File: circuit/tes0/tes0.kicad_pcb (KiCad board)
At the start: 2 copper layers, 21 parts, among them U1 SIM7000E

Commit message: sim7000e minus antena
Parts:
- added J-S70_USIM1: SIM_Card, Connector_Card:microSIM_JAE_SF53S006VCBR2000, F.Cu at (208.7, 116.6)
- moved J-USB-S70 3.43 mm to (189.7, 120.2)
- moved R-S70_USB2 3.35 mm to (190.1, 112.5)
- moved R-S70_USB3 3.35 mm to (188.0, 112.5)
- moved SW-S70-PWR1 3.35 mm to (179.0, 114.9)
- moved SW-S70-RST1 3.35 mm to (168.4, 115.0)
- moved R-S70_USB1 3.35 mm to (192.1, 112.5)
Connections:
- JIO-S3 pad 1: Net-(JIO-S3-Pad1) -> /USIM_VPP
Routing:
- net /S70_USIM_CLK: track 19.3 -> 55.8 mm, vias 0 -> 2
- net /USIM_VPP: track 0.00 -> 34.6 mm
- net /S70_USIM_DATA: track 18.3 -> 46.4 mm, vias 0 -> 2
- net /S70_USIM_VDD: track 17.1 -> 33.6 mm
- net /S70_USIM_RST: track 20.8 -> 36.9 mm
- net GND: track 333.1 -> 347.4 mm
- net /S70_VDD: track 131.4 -> 136.3 mm
- net /S70_USB_DM: track 22.2 -> 25.9 mm
- net /S70_USB_DP: track 24.1 -> 21.1 mm
- net /S70_USB_VBUS: track 32.3 -> 30.7 mm
- net /S70_NRST: track 40.4 -> 38.9 mm
- net Net-(J-USB-S70-Pad2): track 4.04 -> 5.27 mm
- net Net-(J-USB-S70-Pad3): track 5.92 -> 7.10 mm
- net /S70_PWRKEY: track 95.2 -> 94.1 mm
- added copper zone on B.Cu, net (none)
- added copper zone on F.Cu, net (none)
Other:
- board outline added: 66 x 76.4 mm

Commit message: add FT232RL
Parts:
- added C-AMS1: 100nF, Capacitor_SMD:C_0805_2012Metric_Pad1.15x1.40mm_HandSolder, B.Cu at (139.2, 108.1)
- added C-AMS2: 100nF, Capacitor_SMD:C_0805_2012Metric_Pad1.15x1.40mm_HandSolder, B.Cu at (132.8, 108.3)
- added C-FT_3V3: 100nF, Capacitor_SMD:C_0805_2012Metric_Pad1.15x1.40mm_HandSolder, B.Cu at (151.1, 109.4)
- added D-FT_RXD1: LED, LED_SMD:LED_1206_3216Metric_Pad1.42x1.75mm_HandSolder, F.Cu at (141.6, 99.1)
- added D-FT_TXD1: LED, LED_SMD:LED_1206_3216Metric_Pad1.42x1.75mm_HandSolder, F.Cu at (144.2, 99.1)
- added J-BRD_S70_FT1: Conn_02x02_Odd_Even, Connector_PinHeader_2.54mm:PinHeader_2x02_P2.54mm_Vertical, F.Cu at (148.8, 81.4)
- added J-BRD_VDD1: Conn_02x04_Odd_Even, Connector_PinHeader_2.54mm:PinHeader_2x04_P2.54mm_Vertical, F.Cu at (151.1, 52.2)
- added J-FT_USB1: USB_B_Micro, Connector_USB:USB_Micro-B_Wuerth_629105150521, F.Cu at (148.5, 119.7)
- added R-FT_RXD1: 330, Resistor_SMD:R_0805_2012Metric_Pad1.15x1.40mm_HandSolder, B.Cu at (144.2, 99.6)
- added R-FT_TXD1: 330, Resistor_SMD:R_0805_2012Metric_Pad1.15x1.40mm_HandSolder, B.Cu at (141.7, 99.5)
- added U2: FT232RL, Package_SO:SSOP-28_5.3x10.2mm_P0.65mm, F.Cu at (149.8, 107.0)
- added U3: AMS1117-3.3, Package_TO_SOT_SMD:SOT-223-3_TabPin2, F.Cu at (136.1, 108.5)
- renumbered J-USB-S70 to J-S70-USB1
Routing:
- net VDD: track 0.00 -> 135.8 mm, vias 0 -> 4
- net GND: track 347.4 -> 439.2 mm, vias 6 -> 9
- net /FT_RXD: track 0.00 -> 51.3 mm, vias 0 -> 1
- net /S70_VDD: track 136.3 -> 185.9 mm
- net /FT_TXD: track 0.00 -> 45.8 mm, vias 0 -> 1
- net /S70_RXD: track 10.9 -> 28.5 mm, vias 0 -> 1
- net VCC: track 0.00 -> 16.7 mm, vias 0 -> 1
- net /S70_TXD: track 10.5 -> 25.3 mm, vias 0 -> 1
- net Net-(J-FT_USB1-Pad2): track 0.00 -> 13.2 mm
- net Net-(J-FT_USB1-Pad3): track 0.00 -> 12.3 mm
- net Net-(C-FT_3V3-Pad1): track 0.00 -> 9.08 mm, vias 0 -> 1
- net Net-(D-FT_RXD1-Pad2): track 0.00 -> 4.02 mm, vias 0 -> 1
- net Net-(D-FT_TXD1-Pad2): track 0.00 -> 3.92 mm, vias 0 -> 1
- removed copper zone on B.Cu, net (none)
- removed copper zone on F.Cu, net (none)
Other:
- board outline removed

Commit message: update
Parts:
- added C-S70-GPS1: 33pF, Capacitor_SMD:C_0805_2012Metric_Pad1.15x1.40mm_HandSolder, F.Cu at (189.8, 49.1)
- added C-S70-GPS2: 33pF, Capacitor_SMD:C_0805_2012Metric_Pad1.15x1.40mm_HandSolder, F.Cu at (185.7, 49.0)
- added C-S70-GPS3: 10pF, Capacitor_SMD:C_0805_2012Metric_Pad1.15x1.40mm_HandSolder, F.Cu at (198.1, 51.3)
- added C-S70-GPS4: 33pF, Capacitor_SMD:C_0805_2012Metric_Pad1.15x1.40mm_HandSolder, F.Cu at (202.0, 52.7)
- added C-S70_ANT_RF1: C, Capacitor_SMD:C_0805_2012Metric_Pad1.15x1.40mm_HandSolder, B.Cu at (178.6, 64.8)
- added C-S70_ANT_RF2: C, Capacitor_SMD:C_0805_2012Metric_Pad1.15x1.40mm_HandSolder, B.Cu at (182.5, 62.6)
- added FL-S70_GPS1: SAFFA1G58KA0F0A, Filter:Filter_1411-5_1.4x1.1mm, F.Cu at (193.4, 49.2)
- added J-S70_ANT_GPS1: 20279-001E-01, 20279-001E-01:IPEX_20279-001E-01, F.Cu at (180.0, 49.9)
- added J-S70_ANT_RF1: 20279-001E-01, 20279-001E-01:IPEX_20279-001E-01, F.Cu at (172.1, 64.9)
- added L-S70_ANT_RF1: L, Inductor_SMD:L_0805_2012Metric_Pad1.15x1.40mm_HandSolder, B.Cu at (182.4, 64.7)
- added L-S70_GPS1: L, Inductor_SMD:L_0805_2012Metric_Pad1.15x1.40mm_HandSolder, F.Cu at (198.2, 49.2)
- added L-S70_GPS2: L, Inductor_SMD:L_0805_2012Metric_Pad1.15x1.40mm_HandSolder, F.Cu at (189.8, 51.3)
- added L-S70_GPS3: L, Inductor_SMD:L_0805_2012Metric_Pad1.15x1.40mm_HandSolder, F.Cu at (193.7, 47.4)
- added L-S70_GPS4: L, Inductor_SMD:L_0805_2012Metric_Pad1.15x1.40mm_HandSolder, F.Cu at (204.1, 52.7)
- added R-S70-GPS1: 0, Resistor_SMD:R_0805_2012Metric_Pad1.15x1.40mm_HandSolder, F.Cu at (187.6, 47.0)
- added R-S70-GPS2: 10, Resistor_SMD:R_0805_2012Metric_Pad1.15x1.40mm_HandSolder, F.Cu at (185.7, 51.2)
- added R-S70-GPS3: 10, Resistor_SMD:R_0805_2012Metric_Pad1.15x1.40mm_HandSolder, F.Cu at (194.1, 51.3)
- added R-S70_ANT_RF1: 0, Resistor_SMD:R_0805_2012Metric_Pad1.15x1.40mm_HandSolder, B.Cu at (178.5, 62.5)
- added U-S70_GPS1: BGU7005,115, BGU7005_115:PSON50P145X100X50-6N, F.Cu at (202.0, 49.9)
- moved D-FT_TXD1 0.31 mm to (144.2, 98.8)
- moved R-FT_RXD1 0.31 mm to (144.2, 99.3)
- moved R-FT_TXD1 0.31 mm to (141.7, 99.2)
- moved D-FT_RXD1 0.31 mm to (141.6, 98.8)
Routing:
- net GND: track 439.2 -> 537.4 mm, vias 9 -> 12
- net /S70_VDDEXT: track 178.4 -> 212.6 mm
- net /S70_VDD: track 185.9 -> 218.0 mm, vias 3 -> 4
- net Net-(C-S70-GPS3-Pad1): track 0.00 -> 9.36 mm
- net Net-(J-S70_ANT_GPS1-Pad1): track 0.00 -> 7.03 mm
- net /S70_ANT_RF: track 13.9 -> 20.3 mm, vias 0 -> 1
- net /S70_ANT_GPS: track 22.1 -> 27.8 mm
- net Net-(C-S70-GPS1-Pad2): track 0.00 -> 5.23 mm
- net Net-(J-S70_ANT_RF1-Pad1): track 0.00 -> 4.92 mm, vias 0 -> 1
- net Net-(C-S70-GPS1-Pad1): track 0.00 -> 4.30 mm
- net Net-(C-S70-GPS2-Pad2): track 0.00 -> 4.29 mm
- net Net-(C-S70_ANT_RF1-Pad2): track 0.00 -> 4.18 mm
- net /S70_GPS_IN: track 0.00 -> 3.30 mm
- net Net-(L-S70_GPS1-Pad1): track 0.00 -> 2.47 mm
- net Net-(C-S70-GPS4-Pad2): track 0.00 -> 2.06 mm
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- added copper zone on B.Cu, net (none)
- added copper zone on F.Cu, net (none)
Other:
- board outline added: 91.4 x 79.5 mm

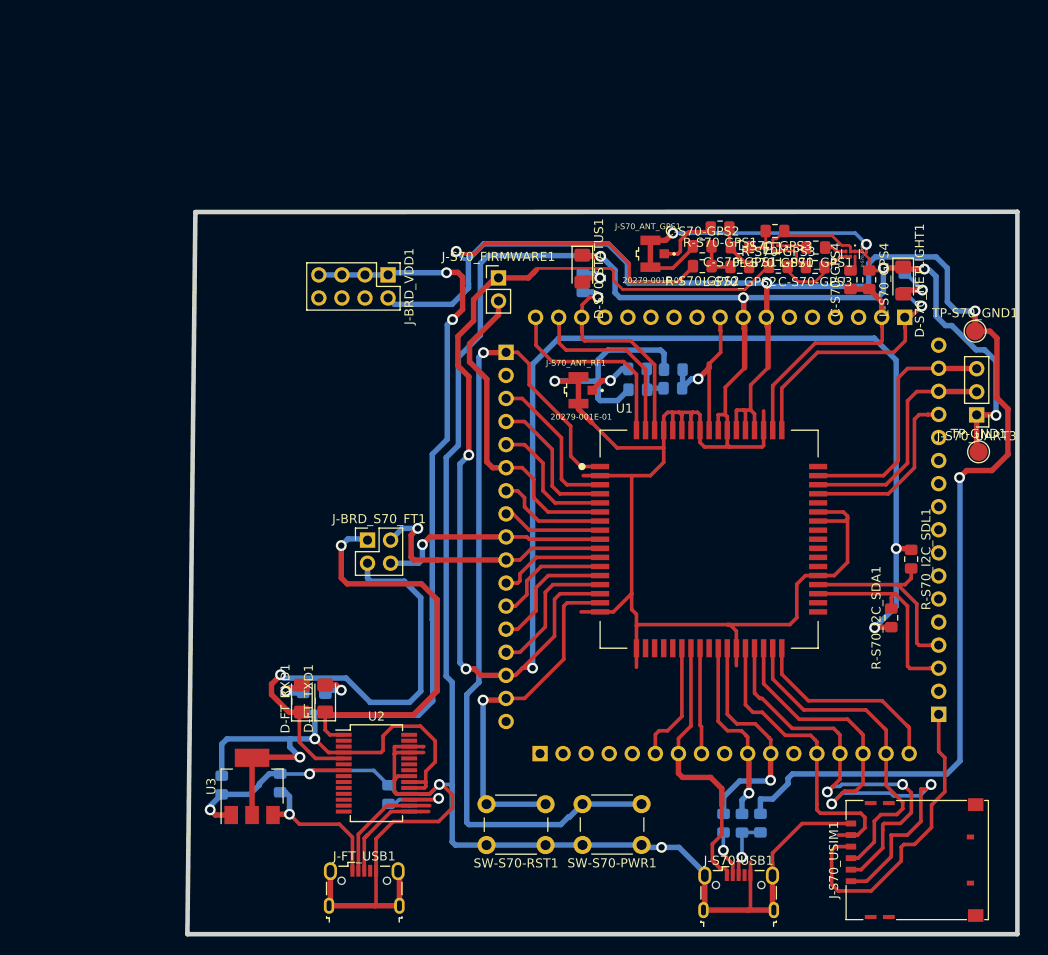
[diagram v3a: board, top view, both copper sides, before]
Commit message: update ikut skematik datasheet
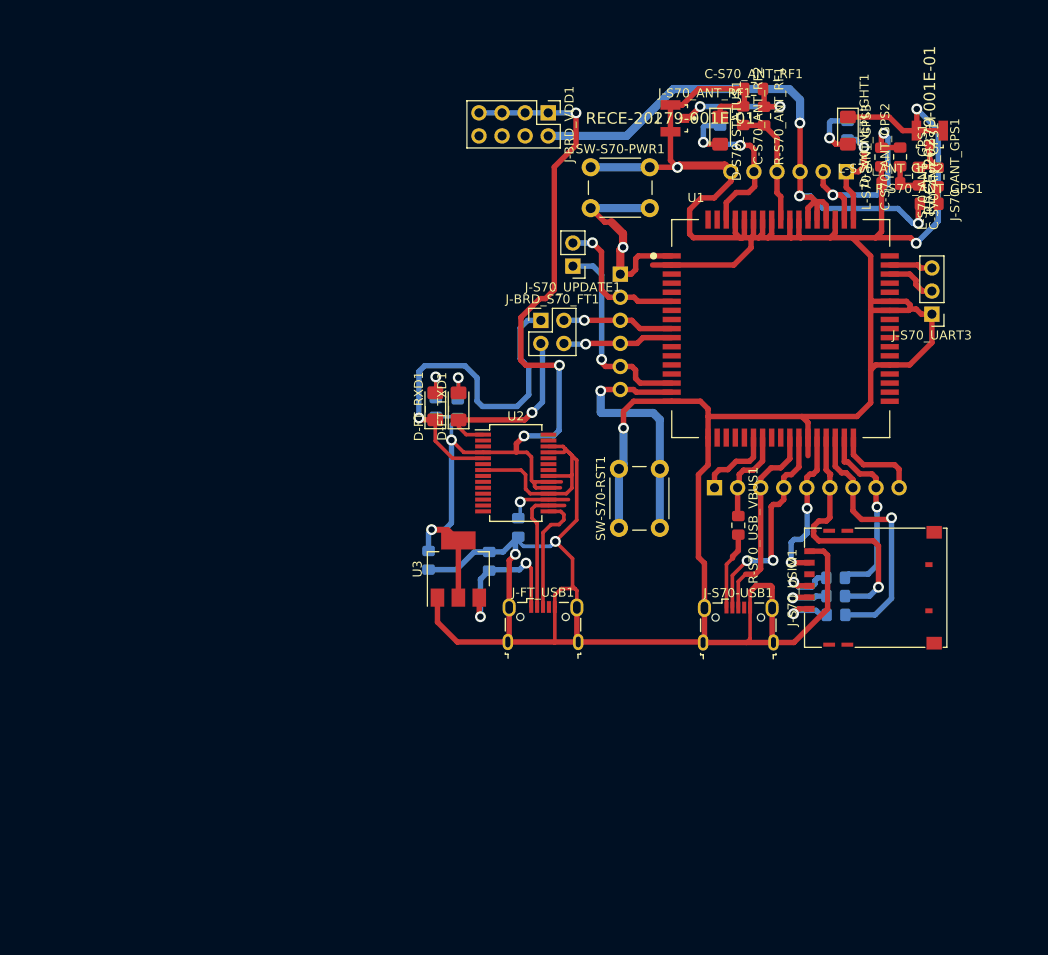
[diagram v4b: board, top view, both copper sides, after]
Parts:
- removed C-S70-GPS1, C-S70-GPS2, C-S70-GPS4: 33pF, Capacitor_SMD:C_0805_2012Metric_Pad1.15x1.40mm_HandSolder
- removed C-S70-GPS3: 10pF, Capacitor_SMD:C_0805_2012Metric_Pad1.15x1.40mm_HandSolder
- removed FL-S70_GPS1: SAFFA1G58KA0F0A, Filter:Filter_1411-5_1.4x1.1mm
- removed J-S70_FIRMWARE1: Conn_01x02_Male, Connector_PinHeader_2.54mm:PinHeader_1x02_P2.54mm_Vertical
- removed JIO-S1, JIO-S2, JIO-S3, JIO-S70: Conn_01x17_Male, Connector_PinHeader_2.54mm:PinHeader_1x17_P2.54mm_Vertical
- removed L-S70_ANT_RF1, L-S70_GPS1, L-S70_GPS2, L-S70_GPS3, L-S70_GPS4: L, Inductor_SMD:L_0805_2012Metric_Pad1.15x1.40mm_HandSolder
- removed R-S70-GPS1: 0, Resistor_SMD:R_0805_2012Metric_Pad1.15x1.40mm_HandSolder
- removed R-S70-GPS2, R-S70-GPS3: 10, Resistor_SMD:R_0805_2012Metric_Pad1.15x1.40mm_HandSolder
- removed R-S70_I2C_SDA1, R-S70_I2C_SDL1, R-S70_USB2: 10K, Resistor_SMD:R_0805_2012Metric_Pad1.15x1.40mm_HandSolder
- removed R-S70_USB1, R-S70_USB3: 68, Resistor_SMD:R_0805_2012Metric_Pad1.15x1.40mm_HandSolder
- removed TP-GND1, TP-S70_GND1: TestPoint_Flag, TestPoint:TestPoint_Pad_D2.0mm
- removed U-S70_GPS1: BGU7005,115, BGU7005_115:PSON50P145X100X50-6N
- added C-S70_ANT_GPS1: 33pF, Capacitor_SMD:C_0805_2012Metric_Pad1.15x1.40mm_HandSolder, F.Cu at (209.5, 41.3)
- added C-S70_ANT_GPS2: 33pF, Capacitor_SMD:C_0805_2012Metric_Pad1.15x1.40mm_HandSolder, F.Cu at (207.5, 39.2)
- added J-S70_PA1: Conn_01x06, Connector_PinHeader_2.54mm:PinHeader_1x06_P2.54mm_Vertical, B.Cu at (176.7, 52.1)
- added J-S70_PB1: Conn_01x09, Connector_PinHeader_2.54mm:PinHeader_1x09_P2.54mm_Vertical, B.Cu at (187.0, 75.6)
- added J-S70_PC1: Conn_01x06, Connector_PinHeader_2.54mm:PinHeader_1x06_P2.54mm_Vertical, B.Cu at (201.5, 40.8)
- added J-S70_UPDATE1: Conn_01x02, Connector_PinHeader_2.54mm:PinHeader_1x02_P2.54mm_Vertical, F.Cu at (171.4, 51.2)
- added L-S70_ANT_GPS1: 47nH, Inductor_SMD:L_0805_2012Metric_Pad1.15x1.40mm_HandSolder, F.Cu at (211.6, 41.4)
- added L-S70_ANT_GPS2: L, Inductor_SMD:L_0805_2012Metric_Pad1.15x1.40mm_HandSolder, F.Cu at (206.4, 42.1)
- added L-S70_ANT_GPS3: L, Inductor_SMD:L_0805_2012Metric_Pad1.15x1.40mm_HandSolder, F.Cu at (205.4, 39.2)
- added R-S70_ANT_GPS1: 10, Resistor_SMD:R_0805_2012Metric_Pad1.15x1.40mm_HandSolder, F.Cu at (210.7, 44.4)
- added R-S70_USB_VBUS1: 0, Resistor_SMD:R_0805_2012Metric_Pad1.15x1.40mm_HandSolder, F.Cu at (189.7, 79.8)
- added R-S70_USIM1: 22, Resistor_SMD:R_0805_2012Metric_Pad1.15x1.40mm_HandSolder, B.Cu at (200.4, 85.5)
- added R-S70_USIM2: 22, Resistor_SMD:R_0805_2012Metric_Pad1.15x1.40mm_HandSolder, B.Cu at (200.4, 89.6)
- added R-S70_USIM3: 22, Resistor_SMD:R_0805_2012Metric_Pad1.15x1.40mm_HandSolder, B.Cu at (200.4, 87.5)
- C-S70_ANT_RF1, C-S70_ANT_RF2, R-S70_ANT_RF1: moved to F.Cu
- J-S70_ANT_GPS1, J-S70_ANT_RF1: value 20279-001E-01 -> RECE-20279-001E-01; footprint 20279-001E-01:IPEX_20279-001E-01 -> eec:Taoglas-RECE-20279-001E-01-MFG
- J-S70_UART3: value Conn_01x03_Male -> Conn_01x03
- moved SW-S70-PWR1 74.8 mm to (173.4, 40.3), turned to 0 degrees
- moved U2 36.4 mm to (165.2, 74.0)
- moved SW-S70-RST1 35.8 mm to (176.5, 80.0), turned to 90 degrees
- moved R-FT_TXD1 35.6 mm to (156.3, 66.8)
- moved R-FT_RXD1 35.5 mm to (158.8, 66.9)
- moved C-S70_ANT_RF1 35.5 mm to (191.3, 31.7)
- moved D-FT_RXD1 35.4 mm to (156.3, 66.6)
- moved D-FT_TXD1 35.3 mm to (158.8, 66.7)
- moved J-FT_USB1 35.1 mm to (168.2, 90.6)
- moved C-AMS2 33.6 mm to (155.6, 83.6)
- moved J-S70_ANT_GPS1 33.6 mm to (210.7, 36.3), turned to 270 degrees
- moved C-AMS1 33.5 mm to (162.2, 83.7)
- moved U3 33.0 mm to (158.8, 84.6)
- moved C-FT_3V3 32.7 mm to (165.4, 80.0), turned to 270 degrees
- moved J-S70_ANT_RF1 31.6 mm to (182.2, 35.0)
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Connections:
- J-BRD_S70_FT1 pad 1: /FT_TXD -> /FT_RXD
- J-BRD_S70_FT1 pad 2: /S70_RXD -> /S70_TXD
- J-BRD_S70_FT1 pad 3: /FT_RXD -> /FT_TXD
- J-BRD_S70_FT1 pad 4: /S70_TXD -> /S70_RXD
- J-S70-USB1 pad 1: /S70_USB_VBUS -> Net-(J-S70-USB1-Pad1)
- J-S70-USB1 pad 2: Net-(J-S70-USB1-Pad2) -> /S70_USB_DM
- J-S70-USB1 pad 3: Net-(J-S70-USB1-Pad3) -> /S70_USB_DP
- J-S70_ANT_RF1 pad 1: Net-(J-S70_ANT_RF1-Pad1) -> Net-(C-S70_ANT_RF1-Pad2)
- J-S70_USIM1 pad 2: /S70_USIM_RST -> Net-(J-S70_USIM1-Pad2)
- J-S70_USIM1 pad 3: /S70_USIM_CLK -> Net-(J-S70_USIM1-Pad3)
- J-S70_USIM1 pad 6: /USIM_VPP -> Net-(J-S70_USIM1-Pad6)
- J-S70_USIM1 pad 7: /S70_USIM_DATA -> Net-(J-S70_USIM1-Pad7)
- R-S70_ANT_RF1 pad 1: Net-(J-S70_ANT_RF1-Pad1) -> Net-(C-S70_ANT_RF1-Pad2)
- R-S70_ANT_RF1 pad 2: Net-(C-S70_ANT_RF1-Pad2) -> /S70_ANT_RF
- U1 pad 11: /S70_PCM_CLK -> Net-(U1-Pad11)
- U1 pad 12: /S70_PCM_SYNC -> Net-(U1-Pad12)
- U1 pad 13: /S70_PCM_DIN -> Net-(U1-Pad13)
- U1 pad 14: /S70_PCM_DOUT -> Net-(U1-Pad14)
- U1 pad 25: /S70_ADC -> Net-(U1-Pad25)
- U1 pad 3: /S70_DTR -> Net-(U1-Pad3)
- U1 pad 37: /S70_I2C_SDA -> Net-(U1-Pad37)
- U1 pad 38: /S70_I2C_SCL -> Net-(U1-Pad38)
- U1 pad 4: /S70_RI -> Net-(U1-Pad4)
- U1 pad 48: /S70_GPIO4 -> Net-(U1-Pad48)
- U1 pad 5: /S70_DCD -> Net-(U1-Pad5)
- U1 pad 67: /S70_GPIO2 -> Net-(U1-Pad67)
- U1 pad 68: /S70_GPIO3 -> Net-(U1-Pad68)
- U1 pad 7: /S70_CTS -> Net-(U1-Pad7)
- U1 pad 8: /S70_RTS -> Net-(U1-Pad8)
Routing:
- net /S70_VDDEXT: track 212.6 -> 22.4 mm, vias 5 -> 1
- net /S70_VDD: track 218.0 -> 66.7 mm, vias 4 -> 3
- net GND: track 537.4 -> 409.5 mm, vias 12 -> 6
- net /S70_PWRKEY: track 94.1 -> 23.0 mm
- net /USIM_VPP: track 34.6 -> 0.00 mm
- net VDD: track 136.3 -> 108.1 mm, vias 4 -> 5
- net /S70_USIM_CLK: track 55.8 -> 28.6 mm, vias 2 -> 1
- net /FT_TXD: track 46.2 -> 20.4 mm
- net /S70_GPIO0: track 28.3 -> 4.78 mm
- net /S70_I2C_SDA: track 23.2 -> 0.00 mm
- net /S70_I2C_SCL: track 22.2 -> 0.00 mm
- net /S70_GPIO3: track 21.9 -> 0.00 mm
- net /S70_GPIO4: track 21.1 -> 0.00 mm
- net /S70_GPIO2: track 20.6 -> 0.00 mm
- net /S70_USB_VBUS: track 30.7 -> 10.5 mm
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- removed copper zone on B.Cu, net (none)
- removed copper zone on F.Cu, net (none)
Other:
- board outline removed

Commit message: basic ESP32+SIM7000
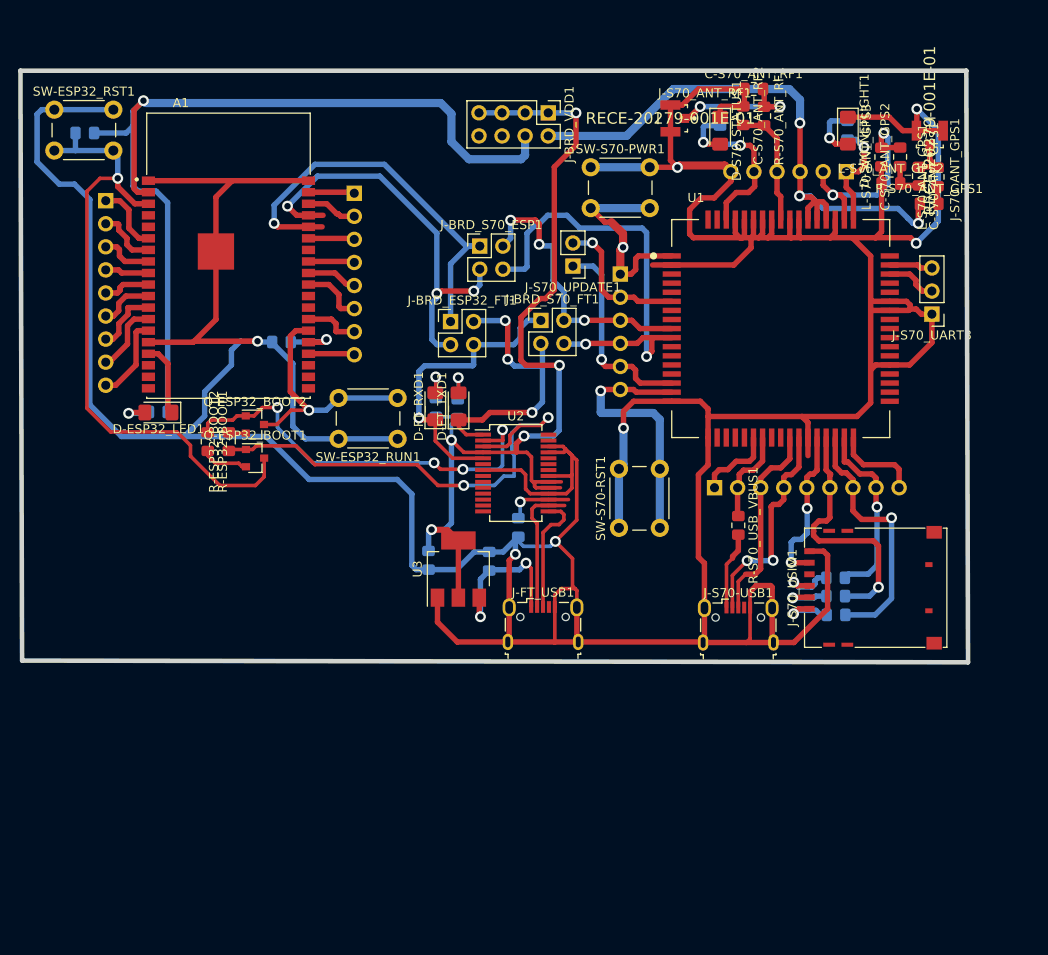
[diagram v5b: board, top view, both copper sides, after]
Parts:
- added A1: ESP32-WROVER-I, esp32-wrover-i:XCVR_ESP32-WROVER-I, F.Cu at (133.5, 50.1)
- added D-ESP32_LED1: LED, LED_SMD:LED_1206_3216Metric_Pad1.42x1.75mm_HandSolder, F.Cu at (125.8, 67.3)
- added J-BRD_ESP32_FT1: Conn_02x02_Odd_Even, Connector_PinHeader_2.54mm:PinHeader_2x02_P2.54mm_Vertical, F.Cu at (158.0, 57.3)
- added J-BRD_S70_ESP1: Conn_02x02_Odd_Even, Connector_PinHeader_2.54mm:PinHeader_2x02_P2.54mm_Vertical, F.Cu at (161.2, 49.0)
- added J-ESP32_PA1: Conn_01x08, Connector_PinHeader_2.54mm:PinHeader_1x08_P2.54mm_Vertical, B.Cu at (147.4, 43.2)
- added J-ESP32_PB1: Conn_01x09, Connector_PinHeader_2.54mm:PinHeader_1x09_P2.54mm_Vertical, B.Cu at (120.0, 44.0)
- added Q-ESP32_BOOT1: 2N3904, Package_TO_SOT_SMD:SOT-23, F.Cu at (136.4, 72.3)
- added Q-ESP32_BOOT2: 2N3904, Package_TO_SOT_SMD:SOT-23, F.Cu at (136.4, 68.7)
- added R-ESP32_BOOT1: 100, Resistor_SMD:R_0805_2012Metric_Pad1.15x1.40mm_HandSolder, F.Cu at (131.2, 70.5)
- added R-ESP32_BOOT2: 100, Resistor_SMD:R_0805_2012Metric_Pad1.15x1.40mm_HandSolder, F.Cu at (133.6, 70.5)
- added R-ESP32_IO2: 10K, Resistor_SMD:R_0805_2012Metric_Pad1.15x1.40mm_HandSolder, B.Cu at (139.4, 59.6)
- added R-ESP32_LED1: 330, Resistor_SMD:R_0805_2012Metric_Pad1.15x1.40mm_HandSolder, B.Cu at (125.8, 67.3)
- added R-ESP32_RST1: 10K, Resistor_SMD:R_0805_2012Metric_Pad1.15x1.40mm_HandSolder, B.Cu at (117.7, 36.6)
- added SW-ESP32_RST1: SW_Push, Button_Switch_THT:SW_PUSH_6mm, F.Cu at (114.3, 34.0)
- added SW-ESP32_RUN1: SW_Push, Button_Switch_THT:SW_PUSH_6mm, F.Cu at (152.1, 70.2)
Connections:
- J-BRD_VDD1 pad 4: Net-(J-BRD_VDD1-Pad4) -> /ESP32_VDD
- U2 pad 2: Net-(U2-Pad2) -> /FT_DTR
- U2 pad 3: Net-(U2-Pad3) -> /FT_RTS
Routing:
- net GND: track 409.5 -> 591.0 mm, vias 6 -> 7
- net /ESP32_VDD: track 0.00 -> 102.7 mm, vias 0 -> 1
- net /ESP32_RST: track 0.00 -> 70.8 mm, vias 0 -> 1
- net /FT_RTS: track 0.00 -> 52.4 mm, vias 0 -> 2
- net /ESP32_RXD: track 0.00 -> 46.1 mm, vias 0 -> 1
- net /ESP32_TXD: track 0.00 -> 45.8 mm, vias 0 -> 3
- net /FT_DTR: track 0.00 -> 45.7 mm, vias 0 -> 4
- net /S70_RXD: track 12.3 -> 49.5 mm, vias 1 -> 2
- net /ESP32_BOOT: track 0.00 -> 27.2 mm, vias 0 -> 1
- net /S70_TXD: track 12.3 -> 31.4 mm, vias 1 -> 3
- net /FT_TXD: track 20.4 -> 32.4 mm, vias 1 -> 3
- net /ESP32_IO12: track 0.00 -> 9.30 mm
- net /FT_RXD: track 42.0 -> 33.1 mm
- net /ESP32_IO14: track 0.00 -> 8.41 mm
- net /ESP32_LED: track 0.00 -> 8.16 mm
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- added copper zone on B.Cu, net (none)
- added copper zone on F.Cu, net (none)
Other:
- board outline added: 104.3 x 65.1 mm
